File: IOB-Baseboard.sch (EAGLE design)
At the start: 21 parts

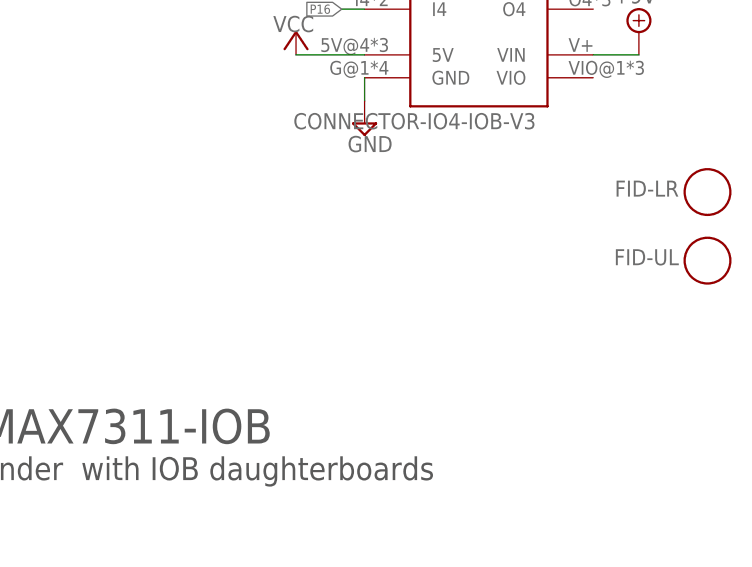
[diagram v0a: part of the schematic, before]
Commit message: added mounting holes
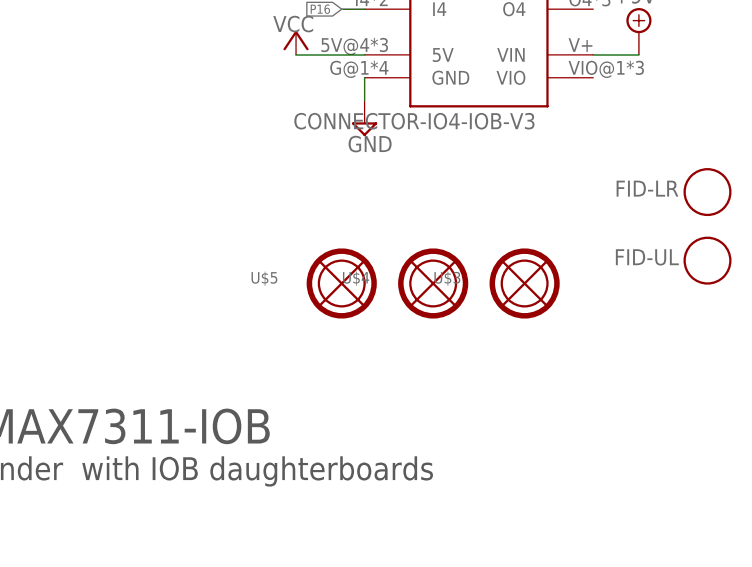
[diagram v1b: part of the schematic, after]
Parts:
- added U$3, U$4, U$5: MOUNTINGHOLE, SPCoast:MOUNTINGHOLE
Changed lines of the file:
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@@
 <part name="V6" library="supply2" deviceset="GND" device=""/>
 <part name="P+6" library="supply1" deviceset="VCC" device=""/>
+<part name="U$3" library="SPCoast" deviceset="MOUNTINGHOLE" device=""/>
+<part name="U$4" library="SPCoast" deviceset="MOUNTINGHOLE" device=""/>
+<part name="U$5" library="SPCoast" deviceset="MOUNTINGHOLE" device=""/>
 </parts>
 <sheets>
@@
 <attribute name="VALUE" x="106.68" y="157.48" size="1.778" layer="96"/>
 </instance>
+<instance part="U$3" gate="MT1" x="223.52" y="45.72"/>
+<instance part="U$4" gate="MT1" x="213.36" y="45.72"/>
+<instance part="U$5" gate="MT1" x="203.2" y="45.72"/>
 </instances>
 <busses>

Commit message: put LEDS back on board, move 2x5 personal;ity and VIO connectors
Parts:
- added LED10, LED11, LED12, LED13, LED14, LED15, LED17, LED19, LED2, LED3, LED4, LED5, LED6, LED7, LED8, LED9: Y, SPCoast:LED0603-LED
- added Q0, Q1, Q10, Q11, Q12, Q13, Q14, Q15, Q2, Q3, Q4, Q5, Q6, Q7, Q8, Q9: P-FET, SPCoast:MOSFET-P-044021001
- added R10, R11, R12, R13, R14, R15, R16, R2, R21, R22, R4, R5, R6, R7, R8, R9: 2K0, SPCoast:R0805-RES
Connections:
- new net N$10: LED8.A, R10.1
- new net N$11: Q8.D, R15.2
- new net N$12: Q9.D, R12.2
- new net N$13: Q10.D, R13.2
- new net N$14: Q11.D, R14.2
- new net N$15: LED13.A, R15.1
- new net N$16: LED10.A, R12.1
- new net N$23: LED11.A, R13.1
- new net N$24: LED12.A, R14.1
- new net N$28: Q12.D, R22.2
- new net N$29: Q13.D, R16.2
- new net N$3: Q4.D, R11.2
- new net N$30: Q14.D, R2.2
- new net N$31: Q15.D, R21.2
- new net N$32: LED19.A, R22.1
- new net N$33: LED14.A, R16.1
- new net N$34: LED15.A, R2.1
- new net N$35: LED17.A, R21.1
- new net N$4: Q5.D, R8.2
- new net N$44: Q0.D, R7.2
- new net N$45: Q1.D, R4.2
- new net N$46: Q2.D, R5.2
- new net N$47: Q3.D, R6.2
- new net N$48: LED5.A, R7.1
- new net N$49: LED2.A, R4.1
- new net N$5: Q6.D, R9.2
- new net N$50: LED3.A, R5.1
- new net N$51: LED4.A, R6.1
- new net N$6: Q7.D, R10.2
- new net N$7: LED9.A, R11.1
- new net N$8: LED6.A, R8.1
- new net N$9: LED7.A, R9.1
- net GND: now also LED10.C, LED11.C, LED12.C, LED13.C, LED14.C, LED15.C, LED17.C, LED19.C, LED2.C, LED3.C, LED4.C, LED5.C, LED6.C, LED7.C, LED8.C, LED9.C
- net P1: now also Q0.G
- net P10: now also Q9.G
- net P11: now also Q10.G
- net P12: now also Q11.G
- net P13: now also Q12.G
- net P14: now also Q13.G
- net P15: now also Q14.G
- net P16: now also Q15.G
- net P2: now also Q1.G
- net P3: now also Q2.G
- net P4: now also Q3.G
- net P5: now also Q4.G
- net P6: now also Q5.G
- net P7: now also Q6.G
- net P8: now also Q7.G
- net P9: now also Q8.G
- net VCC: now also Q0.S, Q1.S, Q10.S, Q11.S, Q12.S, Q13.S, Q14.S, Q15.S, Q2.S, Q3.S, Q4.S, Q5.S, Q6.S, Q7.S, Q8.S, Q9.S
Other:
- note added: "1.1"
- note added: "A"
- note added: "Changes V1.0 - New design, not impacted by I/O wiring movement unseating IOB modules V1.1 - LED dboard was a flop - connector size/cost is expensive"
- note added: "Feedback LEDs"
- note added: "I2C generic Baseboard"
- note added: "IO Expander with IIO personality modules"
- note removed: "Changes V1.0 - New design, not impacted by I/O wiring movement unseating IOB modules"
- note removed: "I2C MAX7311-IOB"
- note removed: "IO Expander with IOB daughterboards"

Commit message: update version text
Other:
- note added: "Changes V1.0 - New design, not impacted by I/O wiring movement unseating IOB modules - LED dboard was a flop - connector size/cost is expensive"
- note removed: "1.1"
- note removed: "Changes V1.0 - New design, not impacted by I/O wiring movement unseating IOB modules V1.1 - LED dboard was a flop - connector size/cost is expensive"
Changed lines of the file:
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@@
 <text x="152.908" y="23.876" size="2.54" layer="97">IO Expander  with IIO personality modules</text>
 <text x="152.908" y="6.35" size="3.81" layer="97">John Plocher</text>
-<text x="235.458" y="6.604" size="3.81" layer="97">1.1</text>
+<text x="235.458" y="6.604" size="3.81" layer="97">1.0</text>
 <text x="149.86" y="38.1" size="1.4224" layer="102">Changes
 V1.0 - New design, not impacted by I/O wiring movement unseating IOB modules
-V1.1 - LED dboard was a flop - connector size/cost is expensive</text>
+     - LED dboard was a flop - connector size/cost is expensive</text>
 </plain>
 <instances>

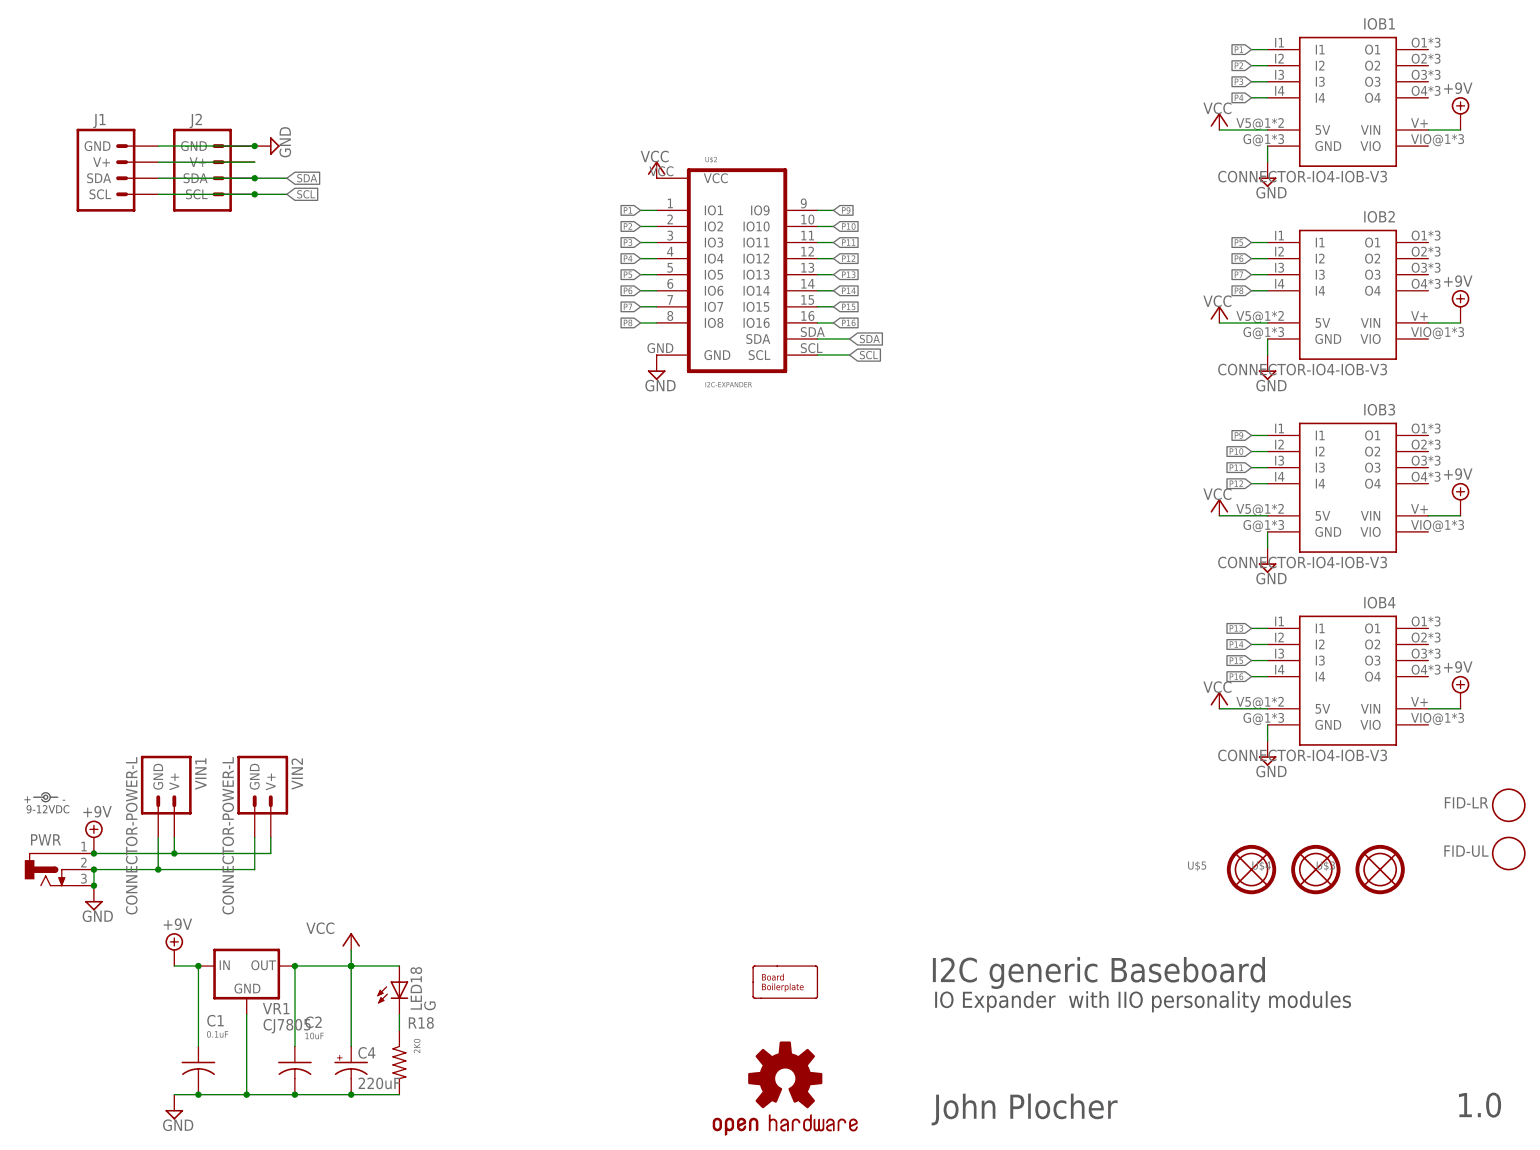
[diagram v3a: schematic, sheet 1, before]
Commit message: added values for connectors
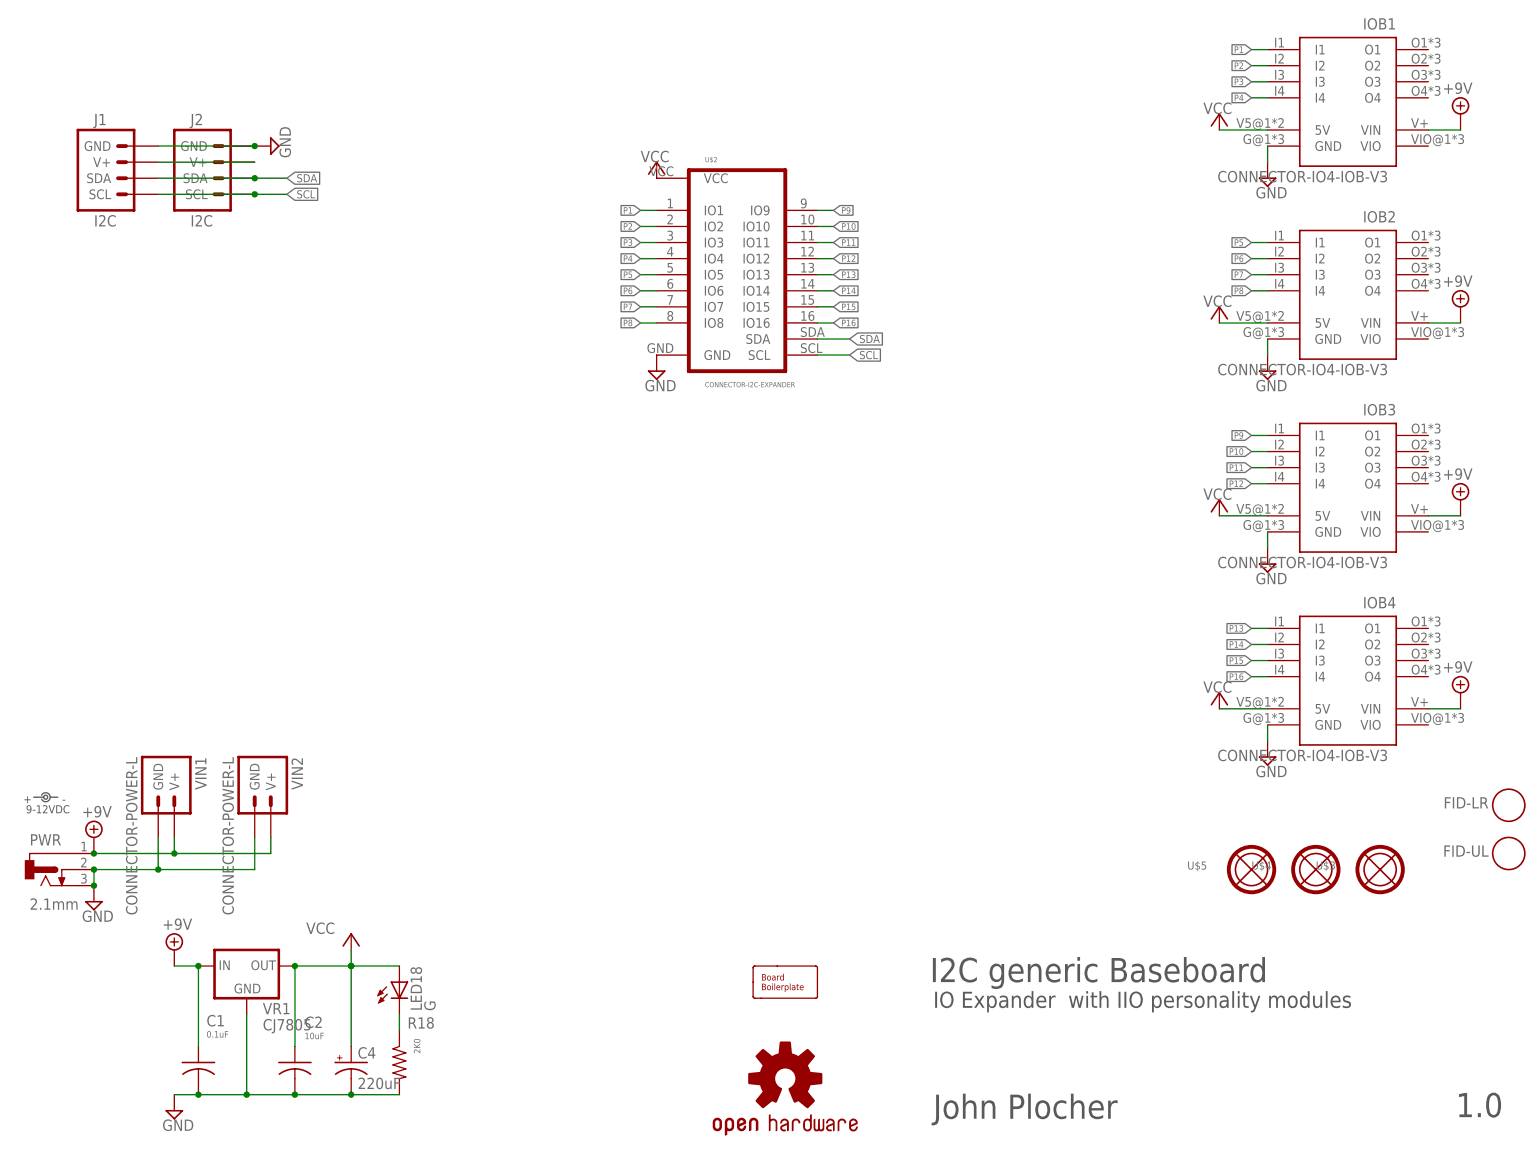
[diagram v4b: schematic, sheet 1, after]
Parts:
- J1, J2: value (none) -> I2C
- PWR: value (none) -> 2.1mm
- U$2: value I2C-EXPANDER -> CONNECTOR-I2C-EXPANDER; device SPCoast:I2C-EXPANDER -> SPCoast:CONNECTOR-I2C-EXPANDER
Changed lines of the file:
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@@
 <layer number="20" name="Dimension" color="15" fill="1" visible="no" active="no"/>
 <layer number="21" name="tPlace" color="19" fill="1" visible="no" active="no"/>
-<layer number="22" name="bPlace" color="22" fill="1" visible="no" active="no"/>
+<layer number="22" name="bPlace" color="17" fill="1" visible="no" active="no"/>
 <layer number="23" name="tOrigins" color="30" fill="1" visible="no" active="no"/>
 <layer number="24" name="bOrigins" color="15" fill="1" visible="no" active="no"/>
@@
 <layer number="46" name="Milling" color="35" fill="1" visible="no" active="no"/>
 <layer number="47" name="Measures" color="21" fill="1" visible="no" active="no"/>
-<layer number="48" name="Document" color="57" fill="1" visible="no" active="no"/>
+<layer number="48" name="Document" color="36" fill="1" visible="no" active="no"/>
 <layer number="49" name="Reference" color="48" fill="1" visible="no" active="no"/>
 <layer number="50" name="dxf" color="7" fill="1" visible="no" active="no"/>
-<layer number="51" name="tDocu" color="49" fill="1" visible="no" active="no"/>
+<layer number="51" name="tDocu" color="24" fill="1" visible="no" active="no"/>
 <layer number="52" name="bDocu" color="7" fill="1" visible="no" active="no"/>
 <layer number="53" name="tGND_GNDA" color="7" fill="9" visible="no" active="no"/>
@@
 <part name="LED18" library="SPCoast" deviceset="LED*" device="0603-LED" value="G"/>
 <part name="SUPPLY2" library="supply2" deviceset="+9V" device=""/>
-<part name="J1" library="SPCoast" deviceset="CONNECTOR-I2C" device="LEFT"/>
-<part name="J2" library="SPCoast" deviceset="CONNECTOR-I2C" device="LEFT"/>
+<part name="J1" library="SPCoast" deviceset="CONNECTOR-I2C" device="LEFT" value="I2C"/>
+<part name="J2" library="SPCoast" deviceset="CONNECTOR-I2C" device="LEFT" value="I2C"/>
 <part name="V12" library="supply2" deviceset="GND" device=""/>
 <part name="BOARD1" library="SPCoast" deviceset="BOARD" device="80X100-IOB" value="BOARD80X100-IOB"/>
@@
 <part name="FID-LR" library="SPCoast" deviceset="FIDUCIAL" device=""/>
 <part name="C4" library="SPCoast" deviceset="CAP-POL*" device="0810" value="220uF"/>
-<part name="PWR" library="SPCoast" deviceset="CONNECTOR-DC-POWER" device="-RA"/>
+<part name="PWR" library="SPCoast" deviceset="CONNECTOR-DC-POWER" device="-RA" value="2.1mm"/>
 <part name="V11" library="supply2" deviceset="GND" device=""/>
 <part name="SUPPLY7" library="supply2" deviceset="+9V" device=""/>
@@
 <part name="SUPPLY5" library="supply2" deviceset="+9V" device=""/>
 <part name="IOB4" library="SPCoast" deviceset="CONNECTOR-IO4-IOB-V3" device=""/>
-<part name="U$2" library="SPCoast" deviceset="I2C-EXPANDER" device=""/>
+<part name="U$2" library="SPCoast" deviceset="CONNECTOR-I2C-EXPANDER" device=""/>
 <part name="V6" library="supply2" deviceset="GND" device=""/>
 <part name="P+6" library="supply1" deviceset="VCC" device=""/>
